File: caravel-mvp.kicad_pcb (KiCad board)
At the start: 4 copper layers, 39 x 54 mm, 57 parts, among them J1 USB_C_Receptacle_USB2.0, J2 Conn_01x02, J3 Conn_02x04_Odd_Even, J4 Conn_01x06, J5 613012243121, J6 Conn_02x18_Odd_Even, SW1 B3U-1000P, SW2 B3U-1000P, U1 Caravel_QFN, U2 W25Q32JVSS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

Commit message: TinyTapeout 1-2-3 version
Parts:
- U1: value Caravel_QFN -> Caravel_QFN_TT3
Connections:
- net /prj_io28 renamed /in7
- J5 pad 1: /prj_io7 -> /out0
- J5 pad 10: /prj_io14 -> /out6
- J5 pad 2: /prj_io8 -> /out1
- J5 pad 3: /prj_io9 -> /out2
- J5 pad 4: /prj_io10 -> /out3
- J5 pad 7: /prj_io11 -> /out4
- J5 pad 8: /prj_io12 -> /out5
- J5 pad 9: /prj_io13 -> /out6
- J6 pad 10: /prj_io20 -> /in3
- J6 pad 11: /prj_io21 -> /sel3
- J6 pad 12: /prj_io22 -> /in4
- J6 pad 13: /prj_io23 -> /sel4
- J6 pad 15: /prj_io25 -> /sel5
- J6 pad 16: /prj_io24 -> /in5
- J6 pad 18: /prj_io26 -> /in6
- J6 pad 19: /prj_io27 -> /sel6
- J6 pad 2: GND -> /in0
- J6 pad 21: /prj_io29 -> /sel7
- J6 pad 23: /prj_io31 -> /sel8
- J6 pad 24: /prj_io30 -> /drv_sel0
- J6 pad 26: /prj_io32 -> /drv_sel1
- J6 pad 27: /prj_io33 -> ser_tx
- J6 pad 28: /prj_io34 -> /slow_clk
- J6 pad 29: /prj_io35 -> ser_rx
- J6 pad 3: /prj_io15 -> /sel0
- J6 pad 31: /prj_io37 -> /ready
- J6 pad 32: /prj_io36 -> /set_clk_div
- J6 pad 4: /prj_io16 -> /in1
- J6 pad 5: /prj_io17 -> /sel1
- J6 pad 7: /prj_io19 -> /sel2
- J6 pad 8: /prj_io18 -> /in2
- U1 pad 11: /prj_io32 -> /out3
- U1 pad 12: /prj_io33 -> /out4
- U1 pad 13: /prj_io34 -> /out5
- U1 pad 14: /prj_io35 -> /out6
- U1 pad 15: /prj_io36 -> /out7
- U1 pad 16: /prj_io37 -> /ready
- U1 pad 2: /prj_io25 -> /in4
- U1 pad 3: /prj_io26 -> /in5
- U1 pad 4: /prj_io27 -> /in6
- U1 pad 41: /prj_io7 -> unconnected-(U1-crvio[7]-Pad41)
- U1 pad 42: /prj_io8 -> /drv_sel0
- U1 pad 43: /prj_io9 -> /drv_sel1
- U1 pad 44: /prj_io10 -> /slow_clk
- U1 pad 45: /prj_io11 -> /set_clk_div
- U1 pad 46: /prj_io12 -> /sel0
- U1 pad 48: /prj_io13 -> /sel1
- U1 pad 50: /prj_io14 -> /sel2
- U1 pad 51: /prj_io15 -> /sel3
- U1 pad 53: /prj_io16 -> /sel4
- U1 pad 54: /prj_io17 -> /sel5
- U1 pad 55: /prj_io18 -> /sel6
- U1 pad 57: /prj_io19 -> /sel7
- U1 pad 58: /prj_io20 -> /sel8
- U1 pad 59: /prj_io21 -> /in0
- U1 pad 6: /prj_io29 -> /out0
- U1 pad 60: /prj_io22 -> /in1
- U1 pad 61: /prj_io23 -> /in2
- U1 pad 62: /prj_io24 -> /in3
- U1 pad 7: /prj_io30 -> /out1
- U1 pad 8: /prj_io31 -> /out2

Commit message: TinyTapeout Stand-alone (no CPU) circuit and info
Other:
- board text added: "v1.1"
- board text removed: "v1.0"
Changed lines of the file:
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@@
   (gr_arc (start 90 79) (mid 89.292893 78.707107) (end 89 78)
     (stroke (width 0.1) (type default)) (layer "Edge.Cuts"))
-  (gr_text "v1.0" (at 119.7 44.4) (layer "F.SilkS")
+  (gr_text "v1.1" (at 119.7 44.4) (layer "F.SilkS")
     (effects (font (size 1 1) (thickness 0.15)) (justify right bottom))
   )

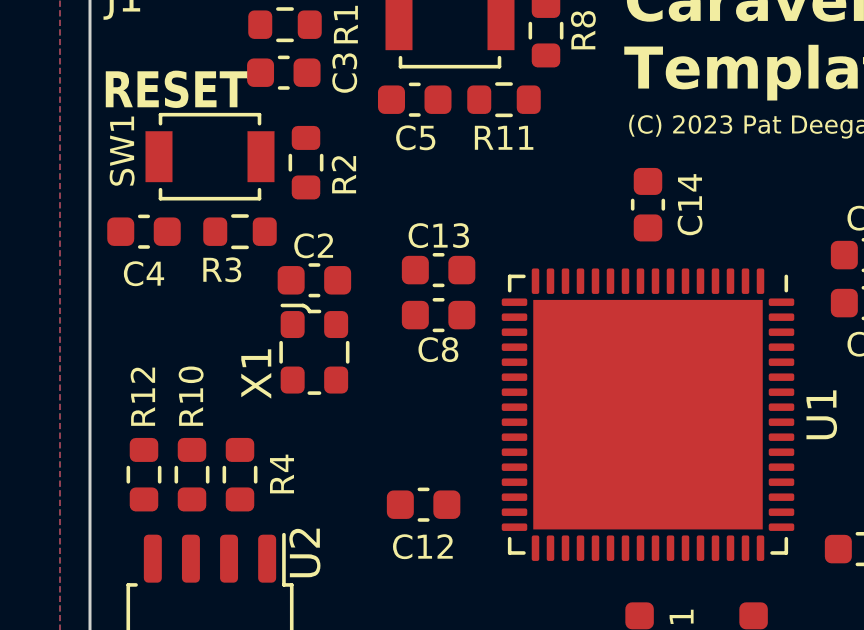
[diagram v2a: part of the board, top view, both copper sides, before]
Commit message: Reset rise and slow clock config fixes
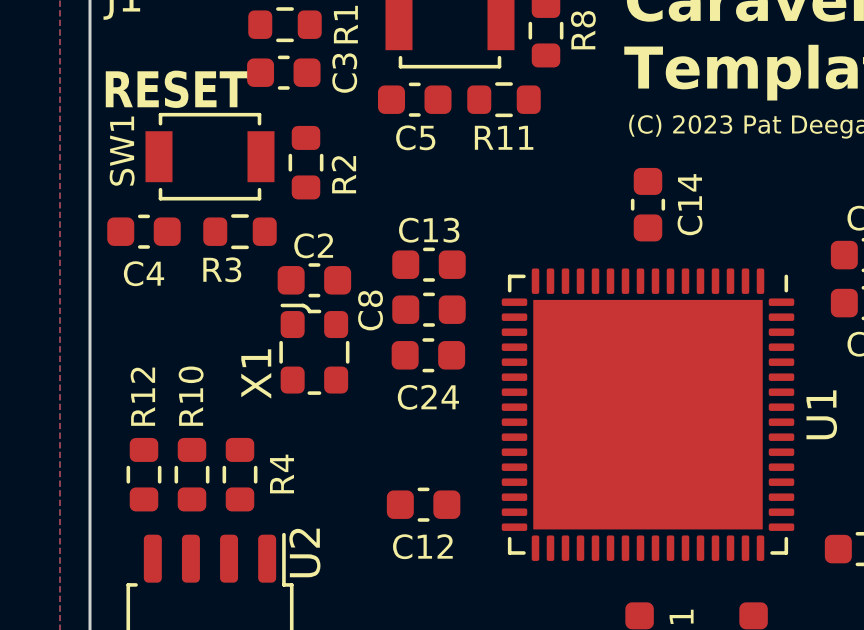
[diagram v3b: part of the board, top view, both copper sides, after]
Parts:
- added C24: 1uF, Capacitor_SMD:C_0603_1608Metric, F.Cu at (100.3, 54.0)
- moved C13 0.37 mm to (100.3, 51.0)
- moved C8 0.37 mm to (100.3, 52.5)
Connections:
- net /drv_sel0 renamed /SCS.DRV_{0}
- net /drv_sel1 renamed /SCS.DRV_{1}
- J5 pad 10: /out6 -> /out7
- J6 pad 28: /slow_clk -> /SCS.slowclk
- J6 pad 32: /set_clk_div -> /SCS.setdiv
- U1 pad 44: /slow_clk -> /slowclk
- U1 pad 45: /set_clk_div -> /setdiv
